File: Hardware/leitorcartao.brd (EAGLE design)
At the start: 34.5 x 56.7 mm, 167 parts, among them IC1 TL084, IC2 TL084, Q1 BSH103, Q2 BC847ASMD, Q3 BC857ALT1SMD, Q4 BC847ALT1SMD, Q5 BC847ALT1SMD, Q6 BC847ALT1SMD, Q7 BC847ALT1SMD, U1 SAMD20E14A-AUT, U3 TLV1117-50CDCYR, U4 MFRC52202HN1, U5 LP2985-33DBVR, X1 ANTENA 125kHz, X2 MIFARE ANTENA

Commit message: Início da versão 3.0
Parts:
- removed C19: 220p, RFiD:C0402
- removed D4: BAV99, RFiD:SOT23
- removed Q2: BC847ASMD, RFiD:SOT23
- removed Q3: BC857ALT1SMD, RFiD:SOT23-BEC
- removed R14, R50: 10k, RFiD:R0402
- removed R15: 20k, RFiD:R0402
- removed R49: 330k, RFiD:R0402
- removed TP1, TP2, TP3, TP4: TESTPOINT, RFiD:TESTPOINT
- added Q8: MMBT4403, RFiD:SOT23
- added Q9: MMBT4401, RFiD:SOT23
- C12: device RFiD:C0603 -> RFiD:C1812
- C13: value 0.1u -> 1n; device RFiD:C0603 -> RFiD:C1206
- C14: device RFiD:C0603 -> RFiD:C1206
- C15: value 2.2n -> 220n; device RFiD:C0603 -> RFiD:C1206
- C16: value 0.1u -> (none); device RFiD:C0603 -> RFiD:C0402
- C18: value 220n -> (none)
- D3: value BAV99 -> US1J-13-F; device RFiD:SOT23 -> RFiD:SMA
- Q1: value BSH103 -> DMN3404
- R4: value 1k -> (none)
- R6: device RFiD:R0603 -> RFiD:R1206
- R7: value 1k -> (none); device RFiD:R0603 -> RFiD:R0402
- R8: value 1M -> 100k
- R9: value 3.9k -> (none)
- moved Q1 113.8 mm to (-32.9, -56.4)
- moved C18 113.3 mm to (-28.5, -50.3), flipped to the top, turned to 0 degrees
- moved C16 111.7 mm to (-28.5, -45.5), turned to 0 degrees
- moved R9 104.7 mm to (-28.5, -40.7), turned to 0 degrees
- moved R7 104.6 mm to (-28.5, -35.9)
- moved IC2 100.9 mm to (-32.4, -49.0), turned to 0 degrees
- moved R4 95.5 mm to (-28.5, -31.1), flipped to the top, turned to 0 degrees
- moved IC1 85.0 mm to (-26.8, -25.1), turned to 0 degrees
- moved C12 10.7 mm to (24.3, 58.4), turned to 180 degrees
- moved C13 8.81 mm to (24.3, 58.4)
- moved C15 8.27 mm to (17.5, 60.0), turned to 180 degrees
- moved D3 5.51 mm to (21.9, 52.1), turned to 0 degrees
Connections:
- removed net N$17: C19.1, C22.2, IC1.1, R10.1, R9.2, TP2.P$1
- removed net N$21: C20.2, C21.2, IC1.8, IC1.9, R12.2, R13.2
- removed net N$26: IC1.10, R14.1, R15.2, TP4.P$1
- removed net N$59: Q2.2, R46.2
- removed net N$65: C45.2, IC2.1, IC2.6, R48.1, TP6.P$1
- removed net N$66: IC2.5, R49.2, R50.1
- removed net OUT1: C26.2, C46.2, IC1.6, IC1.7, R14.2, TP3.P$1
- new net ASK: C18.1, C22.2, C26.2, IC1.7, R10.1, R9.1
- new net FSK/PSK: IC2.1
- net GND: now also C13.2, C16.2, Q8.3; no longer C15.2, C18.2, D3.1, Q3.C
- net N$10: now also IC1.1, IC1.2; no longer C18.1
- net N$12: now also C16.1, R4.2, R7.1, R9.2; no longer C13.2, D3.3
- net N$13: now also C15.1, D3.K; no longer D3.2, R7.2
- net N$14: now also C15.2, IC1.3, R8.1; no longer C15.1, C16.1, R7.1
- net N$15: now also C18.2, IC1.6, R7.2; no longer C19.2, IC1.2, R4.2, R9.1
- net N$16: now also Q9.2, R46.2; no longer C16.2, D4.3, IC1.3, R8.1, TP1.P$1
- net N$23: now also IC2.3; no longer IC1.5
- net N$27: now also IC1.10; no longer IC1.13
- net N$28: now also IC1.8; no longer IC1.14
- net N$40: now also IC2.8; no longer IC2.14
- net N$48: now also Q9.3; no longer Q2.3
- net N$60: now also Q8.2; no longer Q3.E
- net N$64: now also IC1.12; no longer IC2.2
- net N$7: now also Q8.1, Q9.1; no longer Q2.1, Q3.B
- net N$71: now also IC2.7; no longer IC2.8
- net N$72: now also IC2.5; no longer IC2.9
- net N$75: now also IC2.9; no longer IC2.13
- net N$9: now also D3.A
- net N$90: now also C45.2, IC1.14, R48.1, TP6.P$1; no longer IC2.7, R49.1
- net V+: now also C20.2, C21.2, IC1.13, IC1.5, IC1.9, IC2.2, IC2.6, R12.2, R13.2; no longer D4.1, D4.2, IC1.12, IC2.12, IC2.3, R15.1, R50.2
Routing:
- net OUT1: track 19.9 -> 0.00 mm
- net V+: track 57.4 -> 43.7 mm, vias 5 -> 6
- net N$65: track 13.3 -> 0.00 mm, vias 3 -> 0
- net N$21: track 11.9 -> 0.00 mm, vias 2 -> 0
- net N$17: track 9.66 -> 0.00 mm, vias 2 -> 0
- net N$16: track 8.74 -> 0.00 mm, vias 1 -> 0
- net N$26: track 8.37 -> 0.00 mm
- net N$15: track 8.28 -> 0.00 mm, vias 2 -> 0
- net GND: track 55.1 -> 47.0 mm, vias 52 -> 45
- net N$7: track 5.94 -> 0.71 mm, vias 1 -> 0
- net N$9: track 4.43 -> 0.04 mm
- net N$66: track 4.37 -> 0.00 mm, vias 1 -> 0
- net ASK: track 0.00 -> 4.21 mm, vias 0 -> 1
- net N$59: track 4.15 -> 0.00 mm, vias 1 -> 0
- net N$14: track 2.98 -> 0.00 mm
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
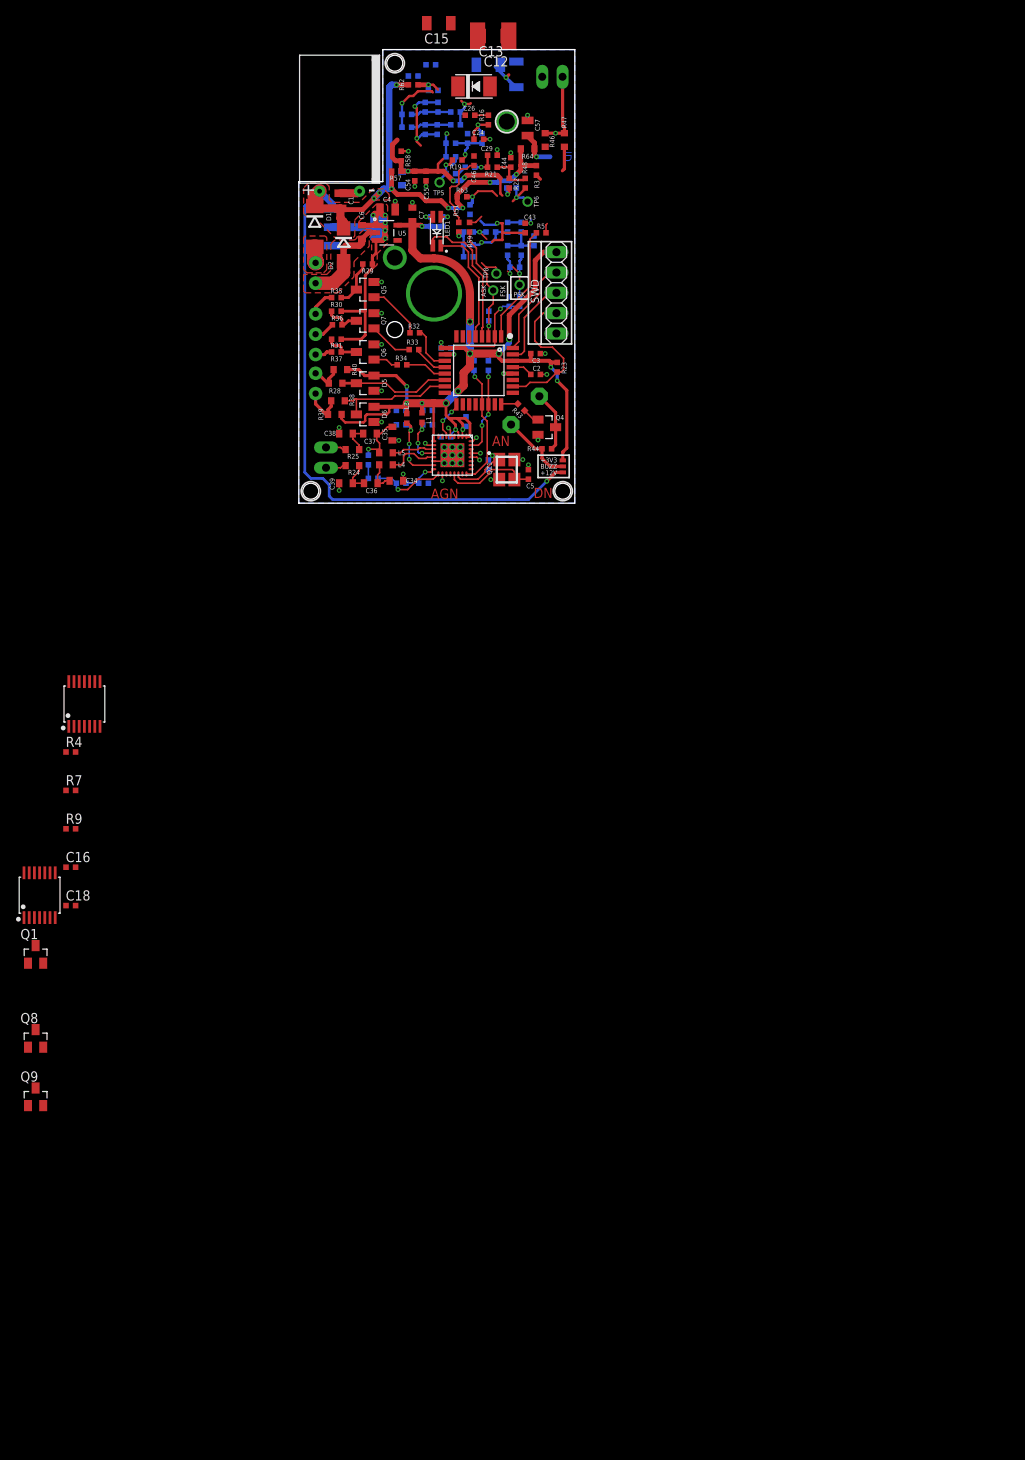
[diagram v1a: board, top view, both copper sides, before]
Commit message: Novas alterações do esquema do RFID. ASK com valores já calculados.
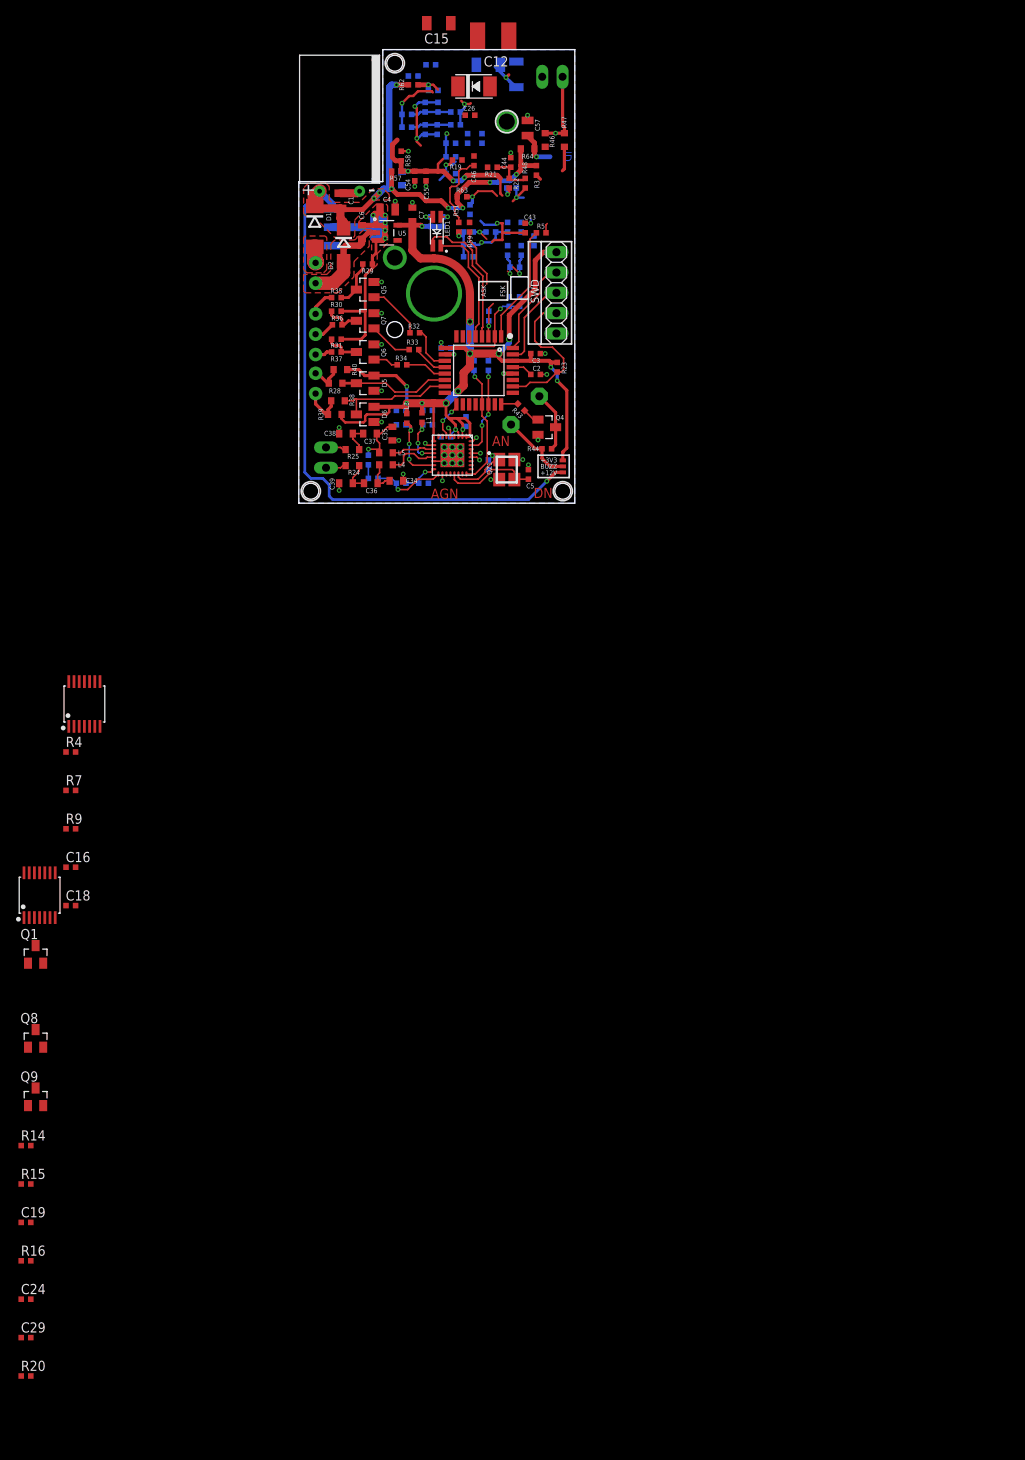
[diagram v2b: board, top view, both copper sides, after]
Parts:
- removed ASK/FSK, PSK, TP5, TP6, TP8: TESTPOINT, RFiD:TESTPOINT
- removed C13: 1n, RFiD:C1206
- added C19: 0.1u, RFiD:C0402
- added R14, R15: (no value), RFiD:R0402
- C24, C29: value 47n -> (none)
- C25, C44: value 4.7n -> 2.2n
- C27, C45: value 22p -> 100p
- C47, C51: value 100p -> (none)
- C48, C50: value 68p -> (none)
- R16, R20: value 220 -> (none)
- R17, R21: value 2k -> 7.5k
- R18, R22: value 9.1k -> 12k
- R19, R48: value 68k -> 150k
- R51, R54: value 5.6k -> (none)
- R52, R55: value 5.1k -> (none)
- R53, R56: value 270k -> (none)
- moved R20 161.0 mm to (-34.1, -109.1), flipped to the top, turned to 0 degrees
- moved C29 158.9 mm to (-34.1, -104.3)
- moved C24 155.7 mm to (-34.1, -99.5)
- moved R16 153.9 mm to (-34.1, -94.7), turned to 0 degrees
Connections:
- removed net N$22 (its old number): C26.1, R16.2
- removed net N$28: C27.1, C28.1, IC1.8, R19.1, TP5.P$1
- new net ASK_MID: C28.2, R21.1
- new net N$17: C20.2, C21.2, R12.2, R13.2, R14.1, R15.2
- new net N$21: C26.1, R17.2
- new net N$26: C24.1, IC2.13, R20.2
- new net N$56: C27.1, C28.1, IC1.8, R19.1
- net ASK-FSK: no longer ASK/FSK.P$1
- net FSK/PSK: now also C46.2, IC2.2, R15.1
- net GND: no longer C13.2, C24.2, C29.2
- net N$24: now also C29.1, IC2.14, R20.1, R60.1; no longer C24.1, R16.1, R17.2
- net N$29: now also C24.2, C29.2, R16.2; no longer C28.2, R20.1
- net N$30: now also C19.1, R16.1; no longer C29.1, R20.2, R21.1
- net N$40: now also C19.2; no longer PSK.P$1, R60.1
- net N$71: no longer TP8.P$1
- net N$9: no longer C13.1
- net N$90: no longer TP6.P$1
- net V+: now also IC2.12, R14.2; no longer C20.2, C21.2, IC2.2, R12.2, R13.2
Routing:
- net N$17: track 0.00 -> 11.1 mm, vias 0 -> 2
- net V+: track 43.7 -> 32.6 mm, vias 6 -> 4
- net N$28: track 6.27 -> 0.00 mm, vias 1 -> 0
- net N$22: track 5.69 -> 0.00 mm, vias 1 -> 0
- net N$56: track 0.00 -> 5.17 mm, vias 0 -> 1
- net N$74: track 5.00 -> 0.00 mm
- net N$24: track 4.61 -> 0.00 mm, vias 1 -> 0
- net N$30: track 3.10 -> 0.00 mm, vias 1 -> 0
- net N$40: track 6.48 -> 3.58 mm
- net N$71: track 8.25 -> 5.43 mm
- net ASK-FSK: track 15.2 -> 12.4 mm
- net N$90: track 7.05 -> 4.53 mm
- net N$25: track 1.70 -> 0.00 mm
- net N$22 (its old number): track 1.70 -> 0.00 mm
- net N$29: track 1.53 -> 0.00 mm
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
